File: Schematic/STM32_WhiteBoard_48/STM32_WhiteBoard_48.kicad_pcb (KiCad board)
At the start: 2 copper layers, 56.8 x 21.4 mm, 41 parts, among them J1 SWDIO+Serial, J2 USB_B_Micro, J3 Header2, J4 Header1, SW1 BOOT0, SW2 RESET, U1 W25Q32JVSSIQ, U2 STM32F103CBTx, U3 LD3985M33R_SOT23, Y1 XC32M4-8.000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

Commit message: Minor layout changes
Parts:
- added G***: LOGO, Icons_Graphics:retronics_logo_14mm, B.Cu at (113.4, 52.8)
- moved R6 4.49 mm to (141.9, 62.3), turned to 90 degrees
- moved D4 1.49 mm to (117.4, 54.5)
- moved R2 1.49 mm to (117.4, 56.1)
- moved D2 0.91 mm to (112.4, 54.5)
- moved R3 0.91 mm to (112.4, 56.1)
- moved R7 0.88 mm to (112.4, 59.3)
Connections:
- J3 pad 1: PA15 -> PA12
- J3 pad 2: PA12 -> PA11
- J3 pad 3: PA11 -> PA10
- J3 pad 4: PA10 -> PA9
- J3 pad 5: PA9 -> PA8
- J3 pad 6: PA8 -> PA15
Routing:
- net PA15: track 37.7 -> 26.2 mm, vias 3 -> 2
- net +3.3V: track 101.8 -> 96.6 mm
- net Net-(U2-OSC_8M_B): track 14.1 -> 19.1 mm
- net PB15: track 17.5 -> 12.7 mm
- net PA12: track 30.1 -> 32.7 mm
- net PA11: track 26.7 -> 29.2 mm
- net PA9: track 20.0 -> 21.7 mm
- net PA10: track 22.5 -> 24.1 mm
- net Net-(U2-OSC_8M_A): track 14.4 -> 13.1 mm
- net GND: track 47.3 -> 46.5 mm, vias 39 -> 35
- net ~{RESET}: track 58.6 -> 59.1 mm
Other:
- board text added: "."
- board text added: "A0"
- board text added: "A1"
- board text added: "A10"
- board text added: "A11"
- board text added: "A12"
- board text added: "A15"
- board text added: "A2"
- board text added: "A3"
- board text added: "A4"
- board text added: "A5"
- board text added: "A6"
- board text added: "A7"
- board text added: "A8"
- board text added: "A9"
- board text added: "B0"
- board text added: "B1"
- board text added: "B10"
- board text added: "B11"
- board text added: "B12"
- board text added: "B13"
- board text added: "B14"
- board text added: "B15"
- board text added: "B2"
- board text added: "B3"
- board text added: "B4"
- board text added: "B5"
- board text added: "B6"
- board text added: "B7"
- board text added: "B8"
- board text added: "B9"
- board text added: "BAT"
- board text added: "C13"
- board text added: "JLCJLCJLCJLC"
- board text added: "STLINK"
- board text added: "locked"
- board text added: "~{RST}"
- board text removed: "3.3V"
- board text removed: "5V"

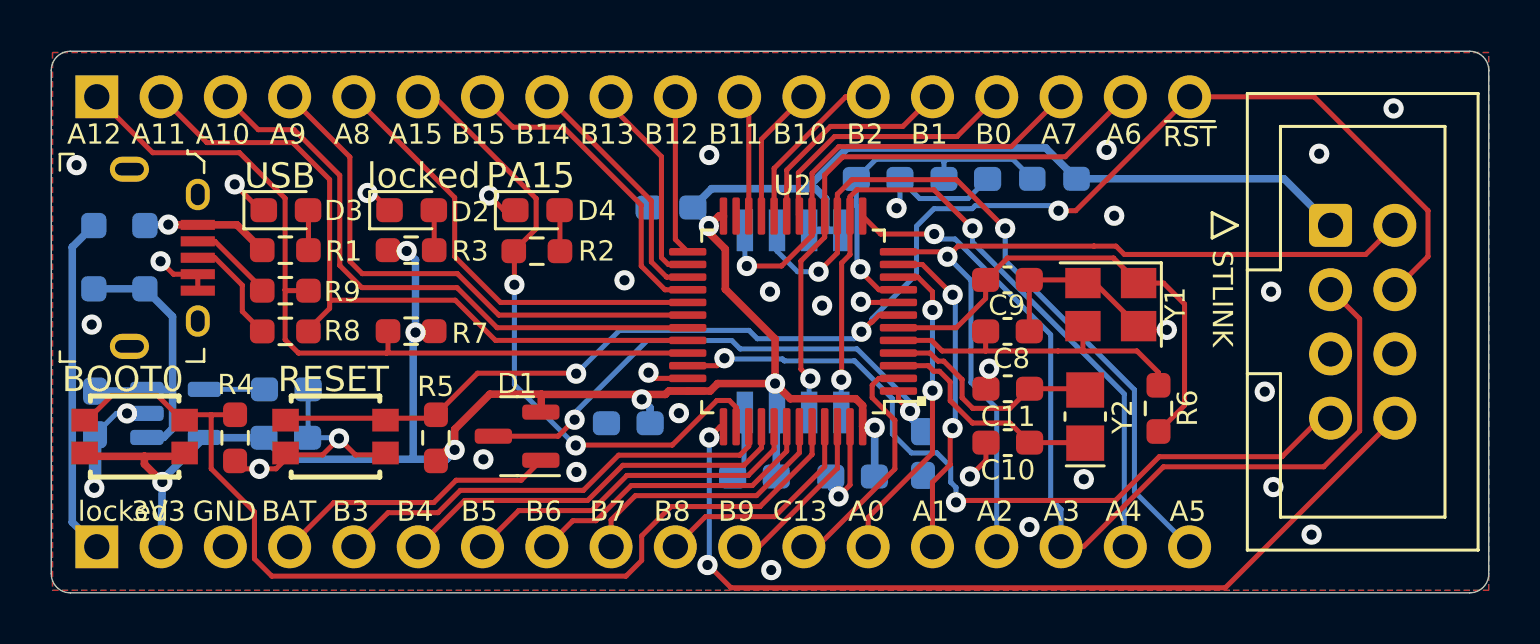
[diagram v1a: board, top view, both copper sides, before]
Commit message: Added ESD protection for USB.
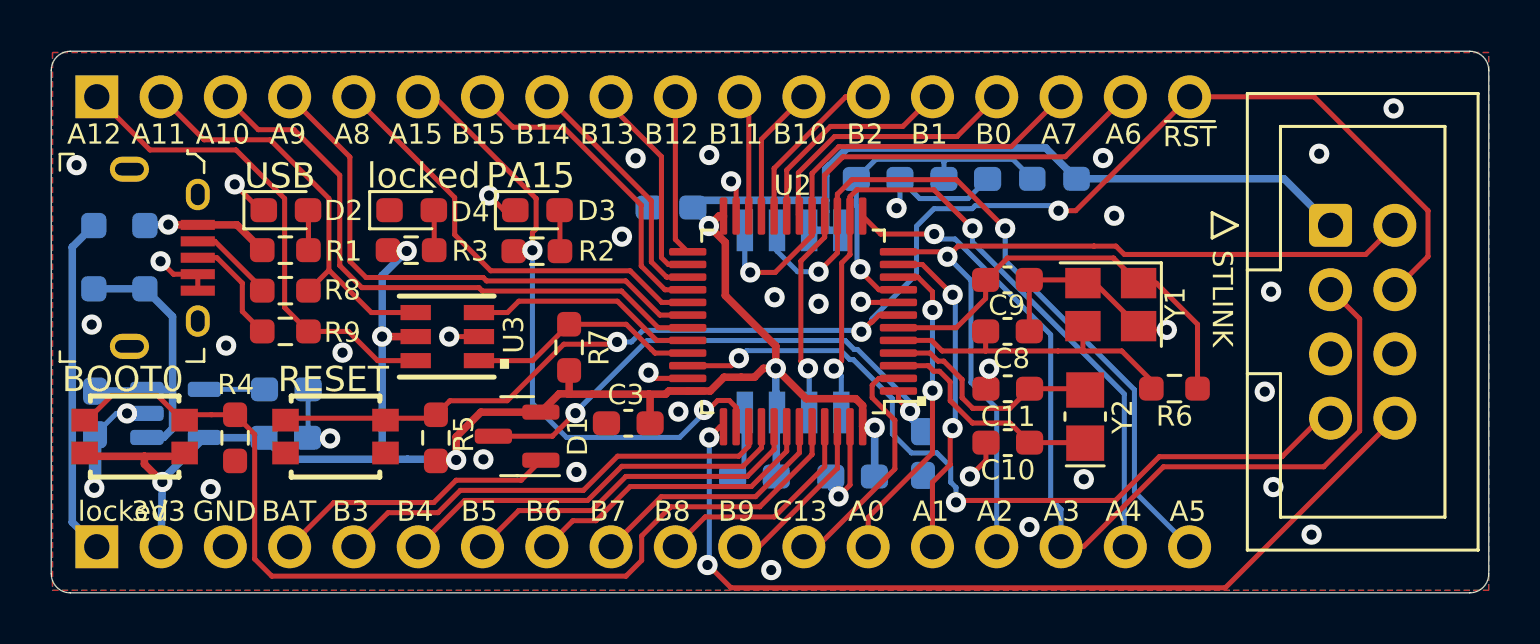
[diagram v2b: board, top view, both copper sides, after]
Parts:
- added U3: USBLC6-2P6, Retronics_IC:USBLC6-2SC6, F.Cu at (113.8, 59.5)
- C3: moved to F.Cu
- J2: footprint digikey-footprints:USB_Micro_B_Female_10118194-0001LF -> Retronics_Connectors:USB_Micro_B_Female_10118194-0001LF
- moved R7 6.28 mm to (118.7, 59.9), turned to 90 degrees
- moved R8 1.61 mm to (107.5, 57.7)
- moved R9 1.61 mm to (107.5, 59.3)
- moved G*** 1.59 mm to (111.8, 52.8)
- moved R6 1.00 mm to (142.6, 61.5), turned to 180 degrees
- renumbered D3 to D2, D4 to D3, D2 to D4, U3 to U4
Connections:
- net PA13 renamed PA13_SWDIO
- net PA14 renamed PA14_SWCLK
- net PA15 renamed PA15_LED
- net PA2 renamed PA2_TX2
- net PA3 renamed PA3_RX2
- net PA4 renamed PA4_CS
- net PA5 renamed PA5_SCK1
- net PA6 renamed PA6_MISO1
- net PA7 renamed PA7_MOSI1
- J3 pad 1: PA12 -> PA12_USB+
- J3 pad 2: PA11 -> PA11_USB-
- R7 pad 2: PA12 -> Net-(U2-PA12_USB+)
- R8 pad 1: PA11 -> PA11_USB-
- R8 pad 2: Net-(J2-D+) -> Net-(J2-D-)
- R9 pad 1: PA12 -> PA12_USB+
- R9 pad 2: Net-(J2-D-) -> Net-(J2-D+)
- U2 pad 32: PA11 -> Net-(U2-PA11_USB-)
- U2 pad 33: PA12 -> Net-(U2-PA12_USB+)
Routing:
- net PA12: track 32.7 -> 0.00 mm
- net PA11: track 29.2 -> 0.00 mm
- net PA12_USB+: track 0.00 -> 19.2 mm
- net PA11_USB-: track 0.00 -> 16.4 mm
- net Net-(U2-PA12_USB+): track 0.00 -> 9.32 mm
- net Net-(U2-PA11_USB-): track 0.00 -> 9.08 mm
- net GND: track 46.5 -> 40.0 mm, vias 35 -> 39
- net +3.3V: track 96.6 -> 98.8 mm, vias 8 -> 7
- net Net-(U2-OSC_8M_B): track 19.1 -> 17.0 mm
- net PB7: track 10.6 -> 10.0 mm
- net PA8: track 17.9 -> 17.4 mm
